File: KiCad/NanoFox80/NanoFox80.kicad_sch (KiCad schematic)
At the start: 78 parts, among them J101 Conn_01x02, J102 Conn_01x02, J103 Conn_01x01, J104 Conn_01x02, J105 Conn_01x02, J106 Conn_01x02, J107 Conn_01x02, J108 Conn_01x01, J109 Conn_01x02, J110 I2C, J111 DB9 Female, J112 Conn_01x02, J113 Conn_01x02, J114 Conn_01x02, P101 ISP/PDI, Q101 BSS84, Q102 BSS138, SW101 SW_SPST, U101 UCC27517DBVR, U102 LP2985-3.3, U103 OPA197, U104 74HC4046, U105 AVR128DA28, U106 74HC390, U107 74HC390, U108 LP2985-5.0, X101 SIT1566AC TCO

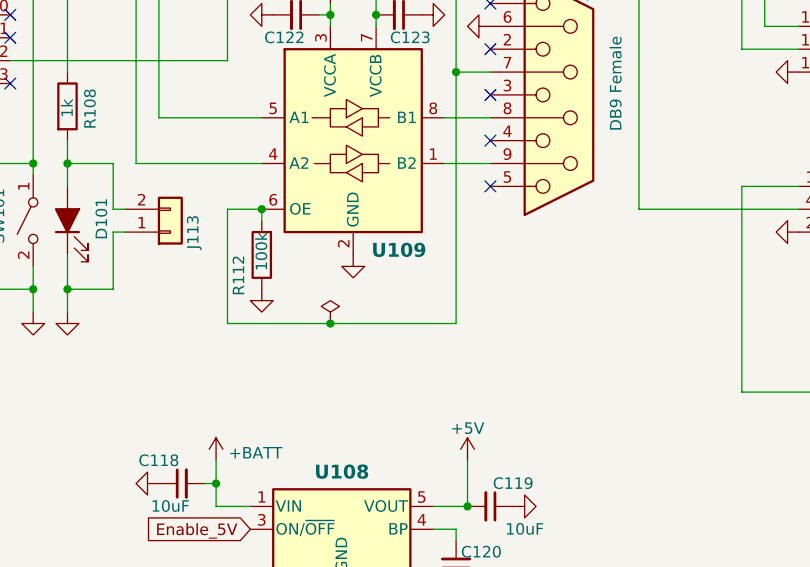
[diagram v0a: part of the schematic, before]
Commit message: Schematic Update
Updated L101 information
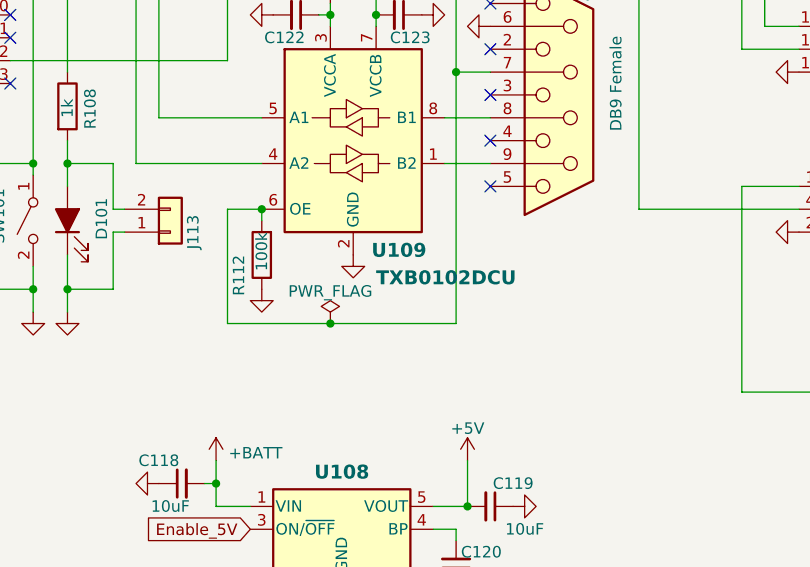
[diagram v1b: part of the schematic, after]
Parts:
- FB101: value (none) -> FerriteBead_Small; footprint (none) -> Inductor_SMD:Ferrite_Bead_NFZ32BW881_Reflow
- L101: Digi-Key Part No. FT50A-43 (Amidon) -> FT-50-67 (Amidon)
- U109: value (none) -> TXB0102DCU; footprint (none) -> Package_SO:VSSOP-8_2.4x2.1mm_P0.5mm
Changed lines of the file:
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@@
       (effects (font (size 1.27 1.27)) hide)
     )
-    (property "Value" "" (id 1) (at 113.03 152.6342 0))
+    (property "Value" "PWR_FLAG" (id 1) (at 113.03 152.6342 0))
     (property "Footprint" "" (id 2) (at 113.03 156.21 0)
       (effects (font (size 1.27 1.27)) hide)
@@
       (effects (font (size 1.27 1.27)) hide)
     )
-    (property "Digi-Key Part No." "FT50A-43 (Amidon)" (id 4) (at 220.98 57.15 0)
+    (property "Digi-Key Part No." "FT-50-67 (Amidon)" (id 4) (at 220.98 57.15 0)
       (effects (font (size 1.27 1.27)) hide)
     )
@@
       (effects (font (size 1.27 1.27)) (justify left))
     )
-    (property "Value" "" (id 1) (at 248.8438 57.5441 0)
+    (property "Value" "FerriteBead_Small" (id 1) (at 248.8438 57.5441 0)
       (effects (font (size 1.27 1.27)) (justify left) hide)
     )
-    (property "Footprint" "" (id 2) (at 244.602 55.88 90)
+    (property "Footprint" "Inductor_SMD:Ferrite_Bead_NFZ32BW881_Reflow" (id 2) (at 244.602 55.88 90)
       (effects (font (size 1.27 1.27)) hide)
     )
@@
       (effects (font (size 1.54 1.54) bold) (justify left))
     )
-    (property "Value" "" (id 1) (at 118.11 151.13 0)
+    (property "Value" "TXB0102DCU" (id 1) (at 118.11 151.13 0)
       (effects (font (size 1.54 1.54) bold) (justify left))
     )
-    (property "Footprint" "" (id 2) (at 115.57 149.86 0)
-      (effects (font (size 1.27 1.27)) hide)
-    )
+    (property "Footprint" "Package_SO:VSSOP-8_2.4x2.1mm_P0.5mm" (id 2) (at 115.57 149.86 0)
+      (effects (font (size 1.27 1.27)) hide)
+    )

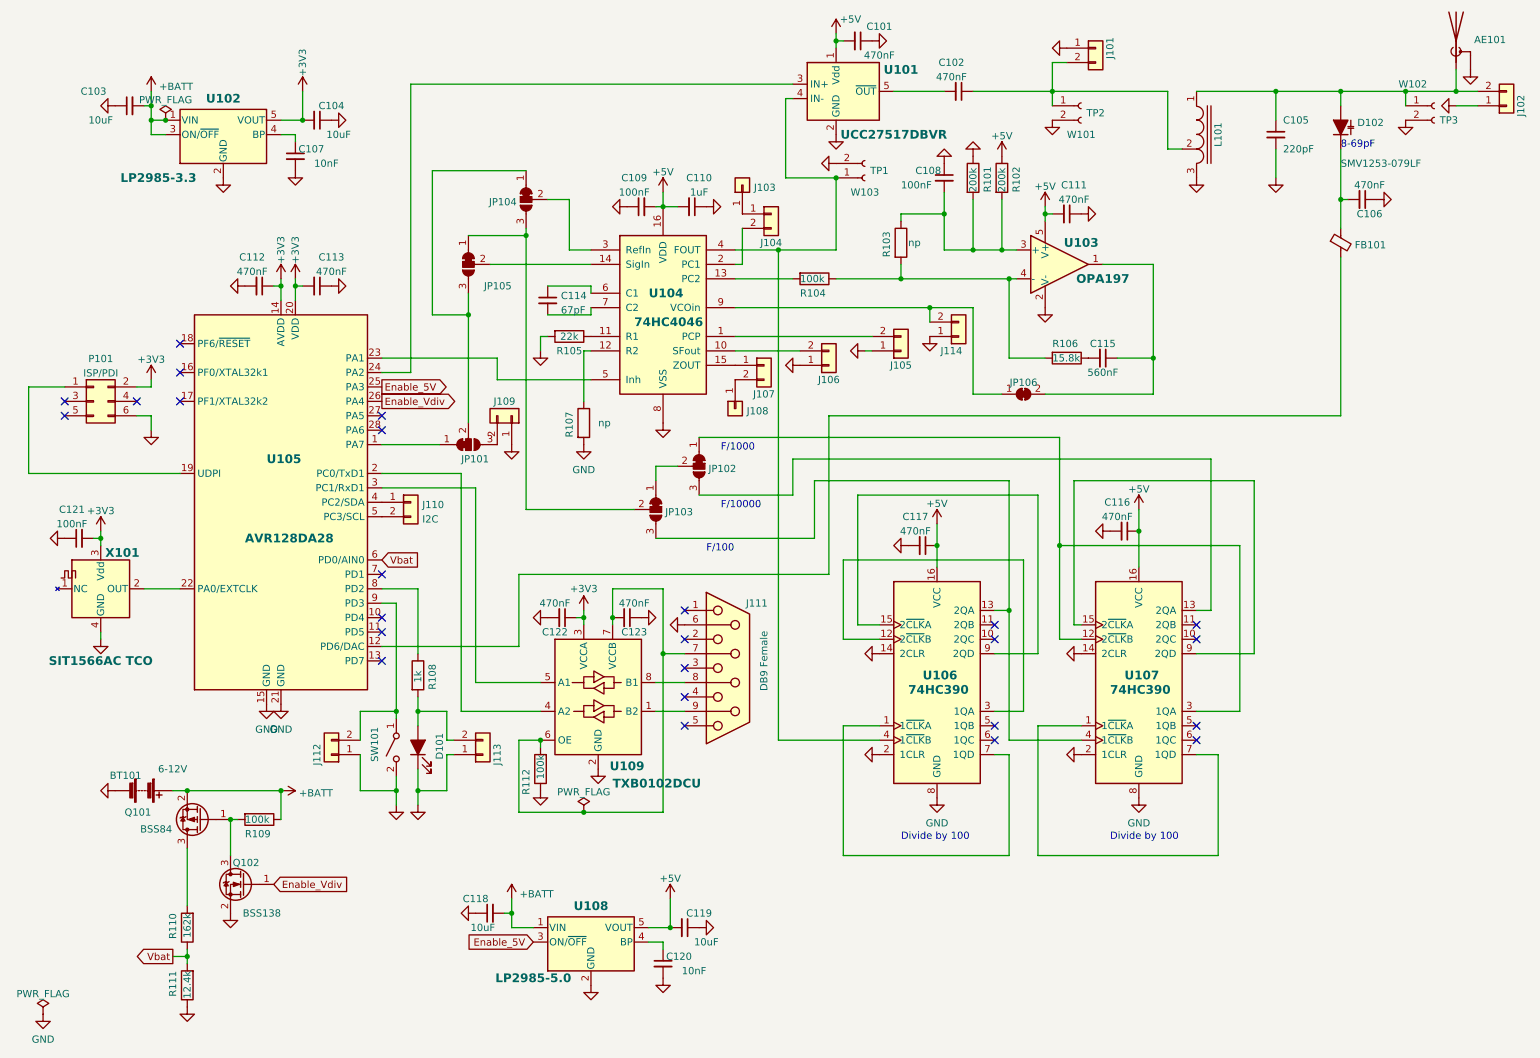
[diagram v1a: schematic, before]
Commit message: Schematic & PCB updates
o Moved X101 connection to U105
o Added header to pin 22 of U105
o Updated schematic and PCB
o Generated new Gerbers
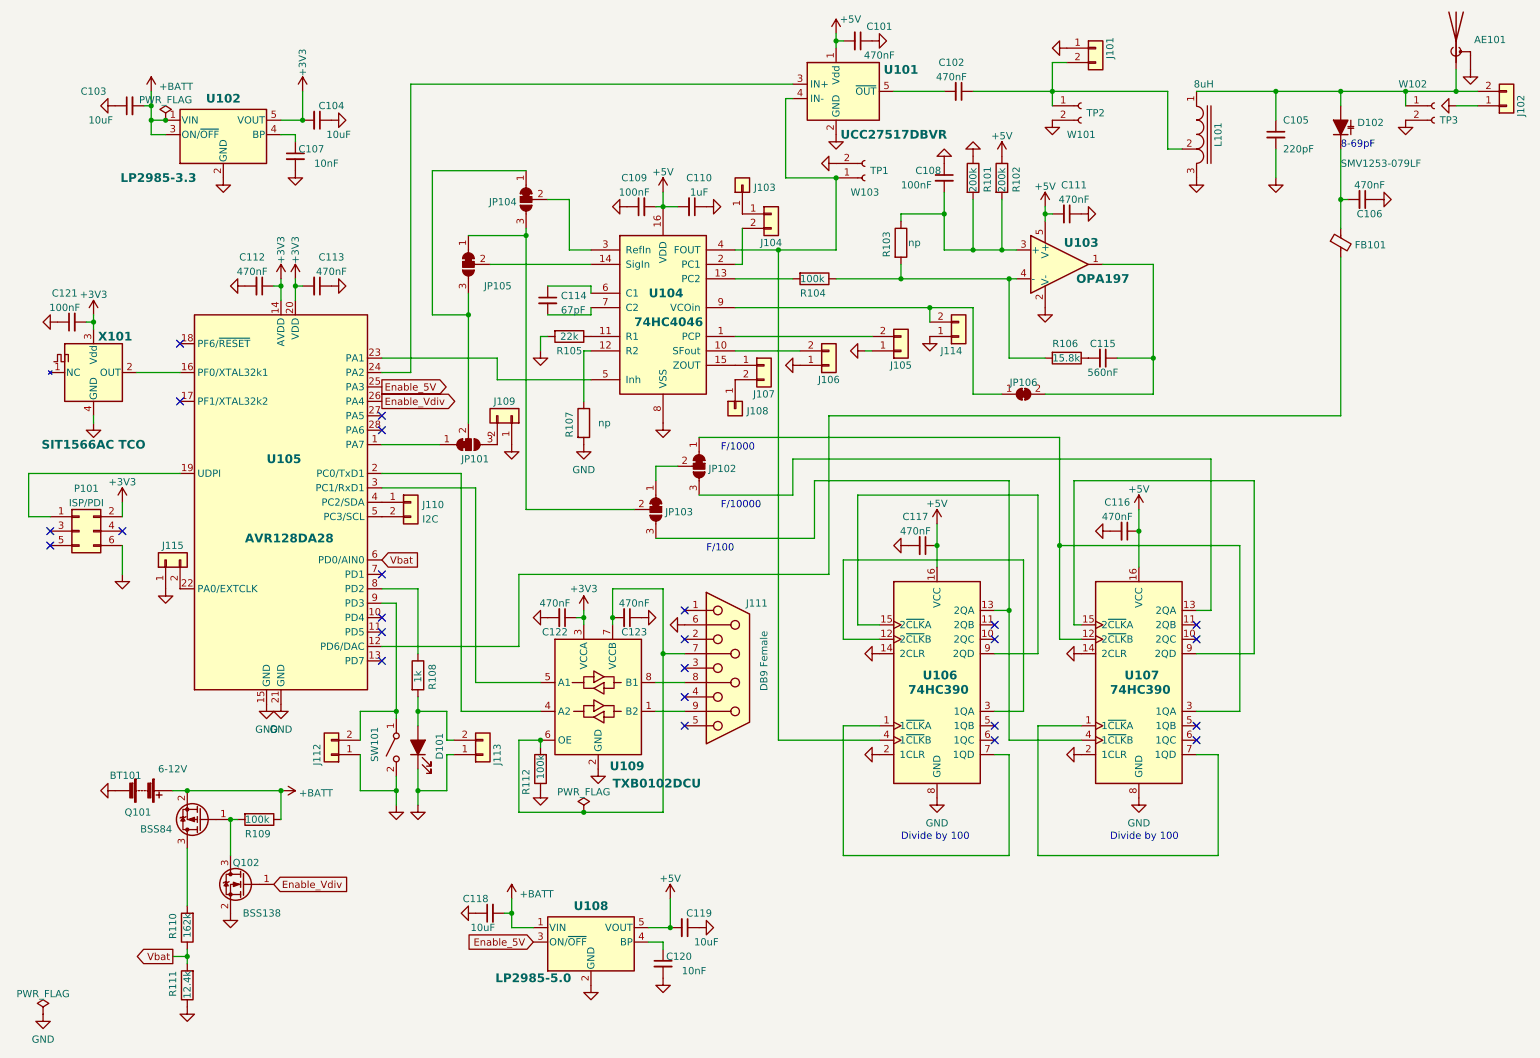
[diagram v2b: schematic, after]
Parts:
- added J115: Conn_01x02, Connector_PinSocket_2.54mm:PinSocket_1x02_P2.54mm_Vertical, symbol Connector_Generic:Conn_01x02
- L101: value (none) -> 8uH; footprint (none) -> Transformer_THT:Autotransformer_Toroid_1Tap_Horizontal_D14.0mm_Amidon-T50
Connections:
- net GND: now also J115.1 (Pin_1)
- net at U105.22 (PA0/EXTCLK): now also J115.2 (Pin_2); no longer X101.2 (OUT)
- net at U105.16 (PF0/XTAL32k1): now also X101.2 (OUT)
- no-connect marks 25 -> 24
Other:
- moved on the sheet: C121, P101, X101

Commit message: Schematic & PCB Updates
o Fixed pinout of Q101
o Changed device for U103
o Corrected PCB for Q101 change
o Updated PCB Rev
o Updated BOM
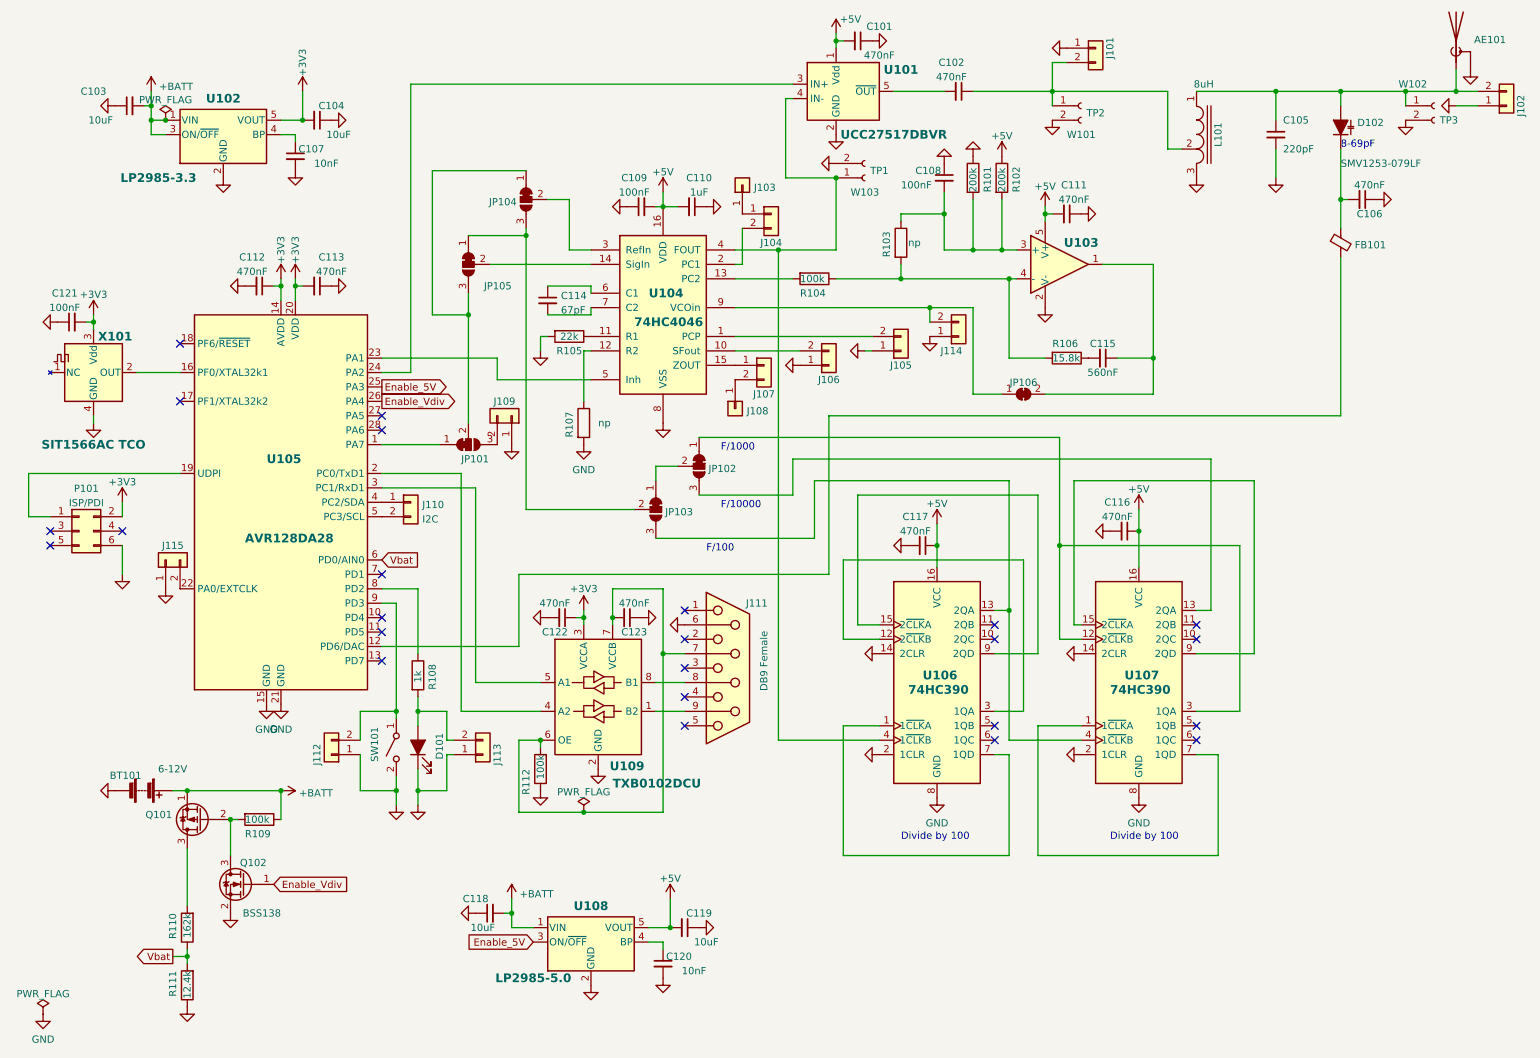
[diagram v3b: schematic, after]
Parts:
- removed Q101: BSS84, Package_TO_SOT_SMD:SOT-23, symbol Transistor_FET:BSS84
- added Q101: (no value), symbol Transistor_FET:BSS84T116
- U103: value OPA197 -> (none); footprint Package_TO_SOT_SMD:SOT-23-5 -> (none); Digi-Key Part No. 296-44109-1-ND -> LMV721M5/NOPBCT-ND; Link (none) -> https://www.digikey.com/en/products/detail/texas-instrument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; Manufacturer PN OPA197IDGKT -> LMV721M5/NOPB
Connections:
- net +BATT: now also Q101.1 (S)
- net at Q102.3 (D), R109.2: now also Q101.2 (G)
- net at R110.2: now also Q101.3 (D)
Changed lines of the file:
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@@
   (junction (at 196.85 109.22) (diameter 0) (color 0 0 0 0)
   )
-  (junction (at 50.8 157.48) (diameter 0) (color 0 0 0 0)
-  )
   (junction (at 147.32 57.15) (diameter 0) (color 0 0 0 0)
   )
@@
   (junction (at 80.01 152.4) (diameter 0) (color 0 0 0 0)
   )
+  (junction (at 43.18 152.4) (diameter 0) (color 0 0 0 0)
+  )
+  (junction (at 50.8 157.48) (diameter 0) (color 0 0 0 0)
+  )
   (junction (at 62.23 63.5) (diameter 0) (color 0 0 0 0)
   )
@@
   (junction (at 246.38 29.21) (diameter 0) (color 0 0 0 0)
   )
-  (junction (at 43.18 152.4) (diameter 0) (color 0 0 0 0)
-  )
   (junction (at 181.61 57.15) (diameter 0) (color 0 0 0 0)
   )
@@
     (stroke (width 0) (type default) (color 0 0 0 0))
   )
+  (wire (pts (xy 43.18 152.4) (xy 59.69 152.4))
+    (stroke (width 0) (type default) (color 0 0 0 0))
+  )
   (wire (pts (xy 86.36 43.18) (xy 102.87 43.18))
     (stroke (width 0) (type default) (color 0 0 0 0))
@@
     (stroke (width 0) (type default) (color 0 0 0 0))
   )
-  (wire (pts (xy 43.18 152.4) (xy 59.69 152.4))
-    (stroke (width 0) (type default) (color 0 0 0 0))
-  )
   (wire (pts (xy 100.33 176.53) (xy 104.14 176.53))
     (stroke (width 0) (type default) (color 0 0 0 0))
@@
       (effects (font (size 1.54 1.54) bold))
     )
-    (property "Value" "OPA197" (id 1) (at 204.47 62.23 0)
+    (property "Value" "" (id 1) (at 204.47 62.23 0)
       (effects (font (size 1.54 1.54) bold))
     )
-    (property "Footprint" "Package_TO_SOT_SMD:SOT-23-5" (id 2) (at 194.31 64.77 0)
+    (property "Footprint" "" (id 2) (at 194.31 64.77 0)
       (effects (font (size 1.27 1.27)) (justify left) hide)
     )
-    (property "Datasheet" "http://www.ti.com/lit/ds/symlink/opa197.pdf" (id 3) (at 196.85 54.61 0)
+    (property "Datasheet" "https://www.ti.com/general/docs/suppproductinfo.tsp?distId=10&gotoUrl=https%3A%2F%2Fwww.ti.com%2Flit%2Fgpn%2Flmv721-n" (id 3) (at 196.85 54.61 0)
       (effects (font (size 1.27 1.27)) hide)
     )
-    (property "Digi-Key Part No." "296-44109-1-ND" (id 4) (at 196.85 59.69 0)
+    (property "Digi-Key Part No." "LMV721M5/NOPBCT-ND" (id 4) (at 196.85 59.69 0)
       (effects (font (size 1.27 1.27)) hide)
     )
@@
       (effects (font (size 1.27 1.27)) hide)
     )
-    (property "Manufacturer PN" "OPA197IDGKT" (id 6) (at 196.85 59.69 0)
+    (property "Manufacturer PN" "LMV721M5/NOPB" (id 6) (at 196.85 59.69 0)
+      (effects (font (size 1.27 1.27)) hide)
+    )
+    (property "Description" "IC OPAMP GP 1 CIRCUIT SOT23-5" (id 7) (at 196.85 59.69 0)
       (effects (font (size 1.27 1.27)) hide)
     )
-    (property "Description" "IC OPAMP GP 1 CIRCUIT 8VSSOP" (id 7) (at 196.85 59.69 0)
+    (property "Link" "https://www.digikey.com/en/products/detail/texas-instruments/LMV721M5-NOPB/364402" (id 8) (at 196.85 59.69 0)
       (effects (font (size 1.27 1.27)) hide)
     )
@@
     (pin "2")
   )
+  (symbol (lib_id "Transistor_FET:BSS84T116") (at 45.72 157.48 180) (unit 1)
+    (in_bom yes) (on_board yes) (fields_autoplaced)
+    (property "Reference" "Q101" (id 0) (at 40.5131 156.6453 0)
+      (effects (font (size 1.27 1.27)) (justify left))
+    )
+    (property "Value" "" (id 1) (at 40.5131 159.1822 0)
+      (effects (font (size 1.27 1.27)) (justify left))
+    )
+    (property "Footprint" "" (id 2) (at 40.64 155.575 0)
+      (effects (font (size 1.27 1.27) italic) (justify left) hide)
+    )
+    (property "Datasheet" "http://assets.nexperia.com/documents/data-sheet/BSS84.pdf" (id 3) (at 45.72 157.48 0)
+      (effects (font (size 1.27 1.27)) (justify left) hide)
+    )
+    (property "Digi-Key Part No." "846-BSS84T116CT-ND" (id 4) (at 45.72 157.48 0)
+      (effects (font (size 1.27 1.27)) hide)
+    )
+    (property "Manufacturer" "Rohm Semiconductor" (id 5) (at 45.72 157.48 0)
+      (effects (font (size 1.27 1.27)) hide)
+    )
+    (property "Manufacturer PN" "BSS84T116" (id 6) (at 45.72 157.48 0)
+      (effects (font (size 1.27 1.27)) hide)
+    )
+    (property "Description" "MOSFET P-CH 60V 230MA SST3" (id 7) (at 45.72 157.48 0)
+      (effects (font (size 1.27 1.27)) hide)
+    )
+    (pin "1")
+    (pin "2")
+    (pin "3")
+  )
   (symbol (lib_id "Device:C_Small") (at 96.52 173.99 90) (mirror x) (unit 1)
     (in_bom yes) (on_board yes)
@@
     (pin "1")
   )
-  (symbol (lib_id "Transistor_FET:BSS84") (at 45.72 157.48 180) (unit 1)
-    (in_bom yes) (on_board yes)
-    (property "Reference" "Q101" (id 0) (at 36.83 156.21 0)
-      (effects (font (size 1.27 1.27)) (justify left))
-    )
-    (property "Value" "BSS84" (id 1) (at 40.5131 159.1822 0)
-      (effects (font (size 1.27 1.27)) (justify left))
-    )
-    (property "Footprint" "Package_TO_SOT_SMD:SOT-23" (id 2) (at 40.64 155.575 0)
-      (effects (font (size 1.27 1.27) italic) (justify left) hide)
-    )
-    (property "Datasheet" "http://assets.nexperia.com/documents/data-sheet/BSS84.pdf" (id 3) (at 45.72 157.48 0)
-      (effects (font (size 1.27 1.27)) (justify left) hide)
-    )
-    (property "Digi-Key Part No." "846-BSS84T116CT-ND" (id 4) (at 45.72 157.48 0)
-      (effects (font (size 1.27 1.27)) hide)
-    )
-    (property "Manufacturer" "Rohm Semiconductor" (id 5) (at 45.72 157.48 0)
-      (effects (font (size 1.27 1.27)) hide)
-    )
-    (property "Manufacturer PN" "BSS84T116" (id 6) (at 45.72 157.48 0)
-      (effects (font (size 1.27 1.27)) hide)
-    )
-    (property "Description" "MOSFET P-CH 60V 230MA SST3" (id 7) (at 45.72 157.48 0)
-      (effects (font (size 1.27 1.27)) hide)
-    )
-    (pin "1")
-    (pin "2")
-    (pin "3")
-  )
   (symbol (lib_id "Device:C_Small") (at 234.95 36.83 0) (unit 1)
     (in_bom yes) (on_board yes)
@@
   (symbol (lib_id "Transistor_FET:BSS138") (at 53.34 168.91 0) (mirror y) (unit 1)
     (in_bom yes) (on_board yes)
-    (property "Reference" "Q102" (id 0) (at 55.88 165.1 0)
+    (property "Reference" "Q102" (id 0) (at 57.15 165.1 0)
       (effects (font (size 1.27 1.27)) (justify left))
     )
@@
       (reference "P101") (unit 1) (value "ISP/PDI") (footprint "Connector_PinHeader_2.54mm:PinHeader_2x03_P2.54mm_Vertical_SMD")
     )
-    (path "/a9d01109-ee71-4ed8-bb46-2d54f0d937f1"
-      (reference "Q101") (unit 1) (value "BSS84") (footprint "Package_TO_SOT_SMD:SOT-23")
+    (path "/a295d13a-ff5b-4b53-92ad-a66323f160b9"
+      (reference "Q101") (unit 1) (value "BSS84T116") (footprint "Package_TO_SOT_SMD:SOT-23")
     )
     (path "/c8819402-7151-4b21-9689-27976a72a03f"
@@
     )
     (path "/6a87be2e-f259-416b-aadf-e12b9d44875b"
-      (reference "U103") (unit 1) (value "OPA197") (footprint "Package_TO_SOT_SMD:SOT-23-5")
+      (reference "U103") (unit 1) (value "LMV721M5") (footprint "Package_TO_SOT_SMD:SOT-23-5")
     )
     (path "/431da72b-e35a-432f-9a9f-c4709ce3697c"
